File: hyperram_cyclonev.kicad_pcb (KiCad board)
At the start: 2 copper layers, 90.1 x 89.7 mm, 57 parts, among them IC1 AP63205WU, IC2 TXB0108PWR, IC3 S26KL128SDABHI020, IC4 W25Q32JVSSIQ_TR, IC5 S27KL0641DABHI020, J1 ASP-122952-01, J2 HDMI_A, J3 Conn_02x10_Odd_Even, J4 Conn_02x06_Odd_Even, J5 Conn_02x06_Top_Bottom, J6 Conn_02x06_Top_Bottom, J7 Conn_02x06_Top_Bottom, Q1 BSS138, Q2 BSS138

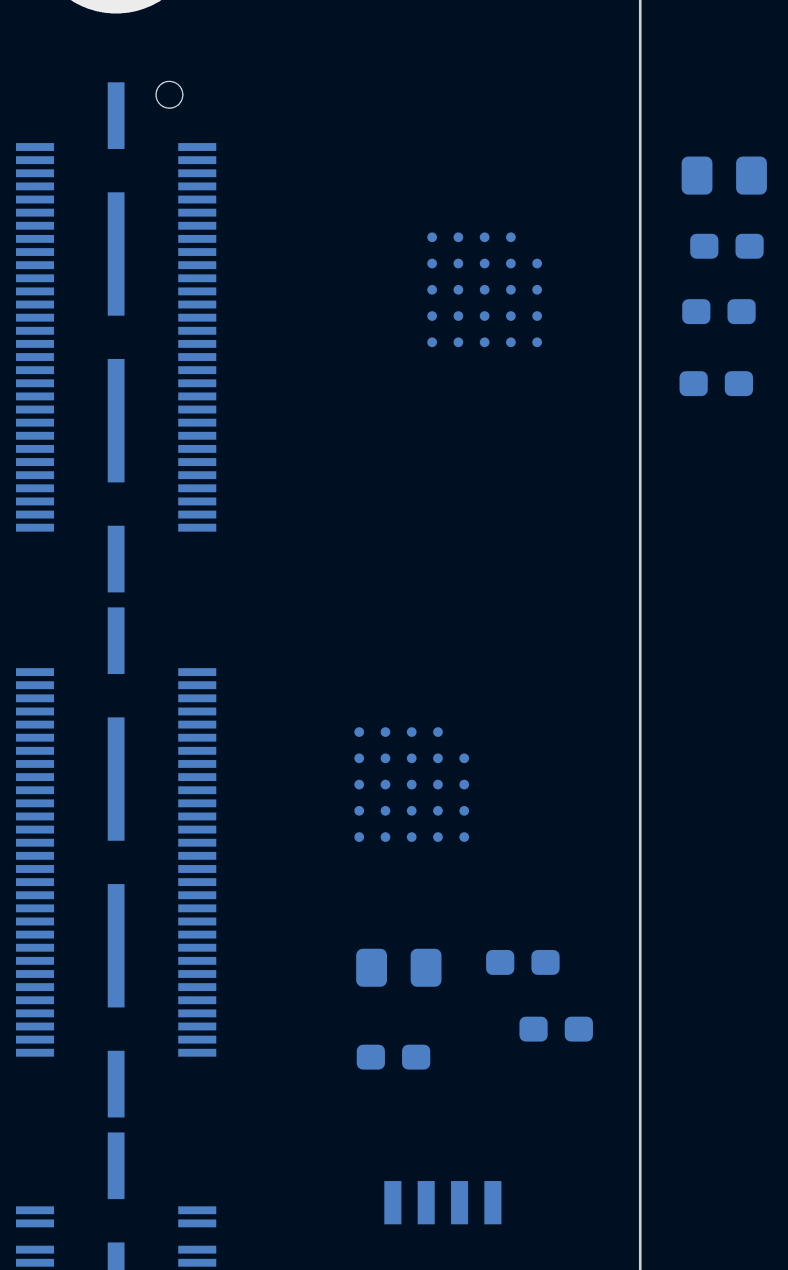
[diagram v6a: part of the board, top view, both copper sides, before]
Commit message: Set constraints for PCBWay: 6/6mil, hole 0.25mm. First try for routing HyperRAM with trace length matching.
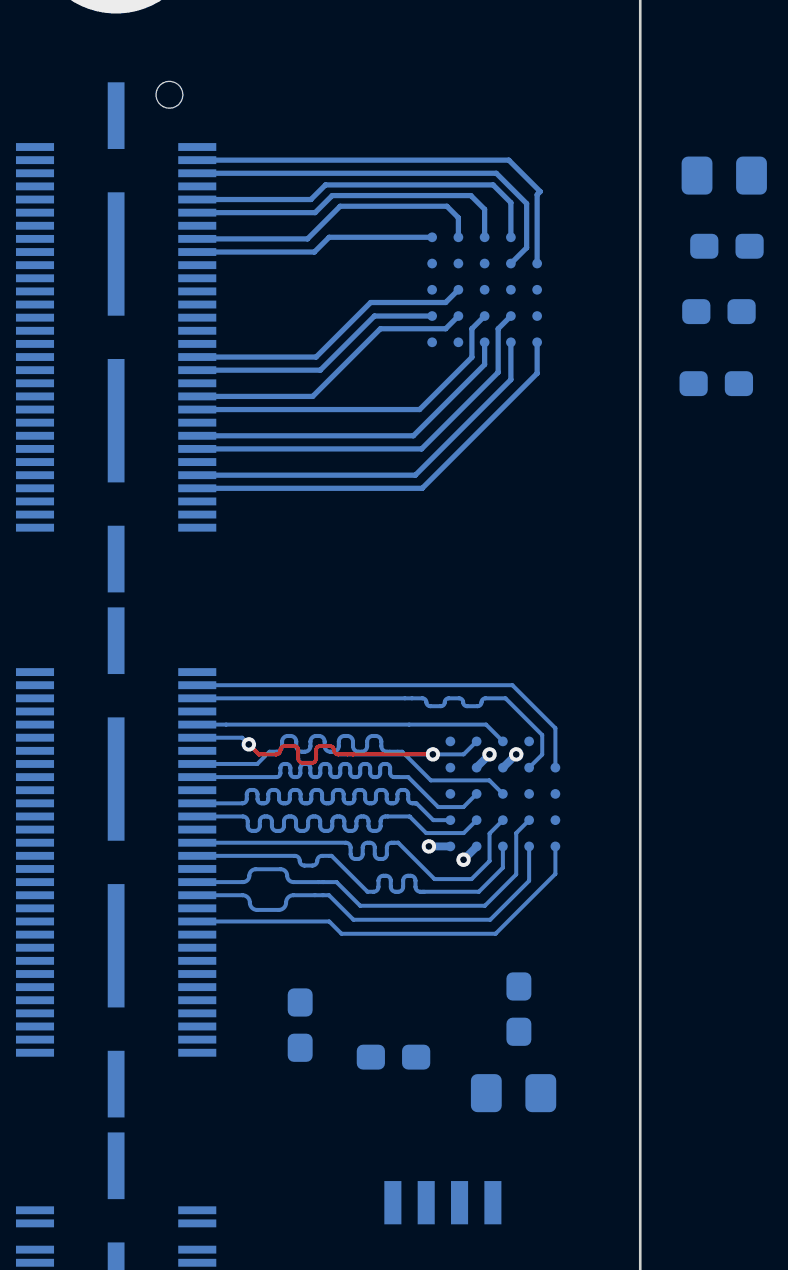
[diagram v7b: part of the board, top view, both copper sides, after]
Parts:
- moved C15 9.75 mm to (229.5, 119.4), turned to -90 degrees
- moved C11 6.47 mm to (237.6, 122.0)
- moved IC5 3.49 mm to (237.2, 110.6)
- moved C14 1.78 mm to (237.8, 118.8), turned to 90 degrees
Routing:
- net /hr2_clkn: track 0.00 -> 16.3 mm
- net /hr2_dq7: track 0.00 -> 15.9 mm
- net /hr1_dq7: track 0.00 -> 15.8 mm
- net /hr1_clkn: track 0.00 -> 15.8 mm
- net /hr1_dq1: track 0.00 -> 15.8 mm
- net /hr1_clkp: track 0.00 -> 15.8 mm
- net /hr1_rwds: track 0.00 -> 15.7 mm
- net /hr1_dq3: track 0.00 -> 15.6 mm
- net /hr1_dq2: track 0.00 -> 15.6 mm
- net /hr1_dq4: track 0.00 -> 15.6 mm
- net /hr2_clkp: track 0.00 -> 15.6 mm
- net /hr1_dq0: track 0.00 -> 15.6 mm
- net /hr1_dq6: track 0.00 -> 15.5 mm
- net /hr1_dq5: track 0.00 -> 15.5 mm
- net /hr2_dq1: track 0.00 -> 15.0 mm
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
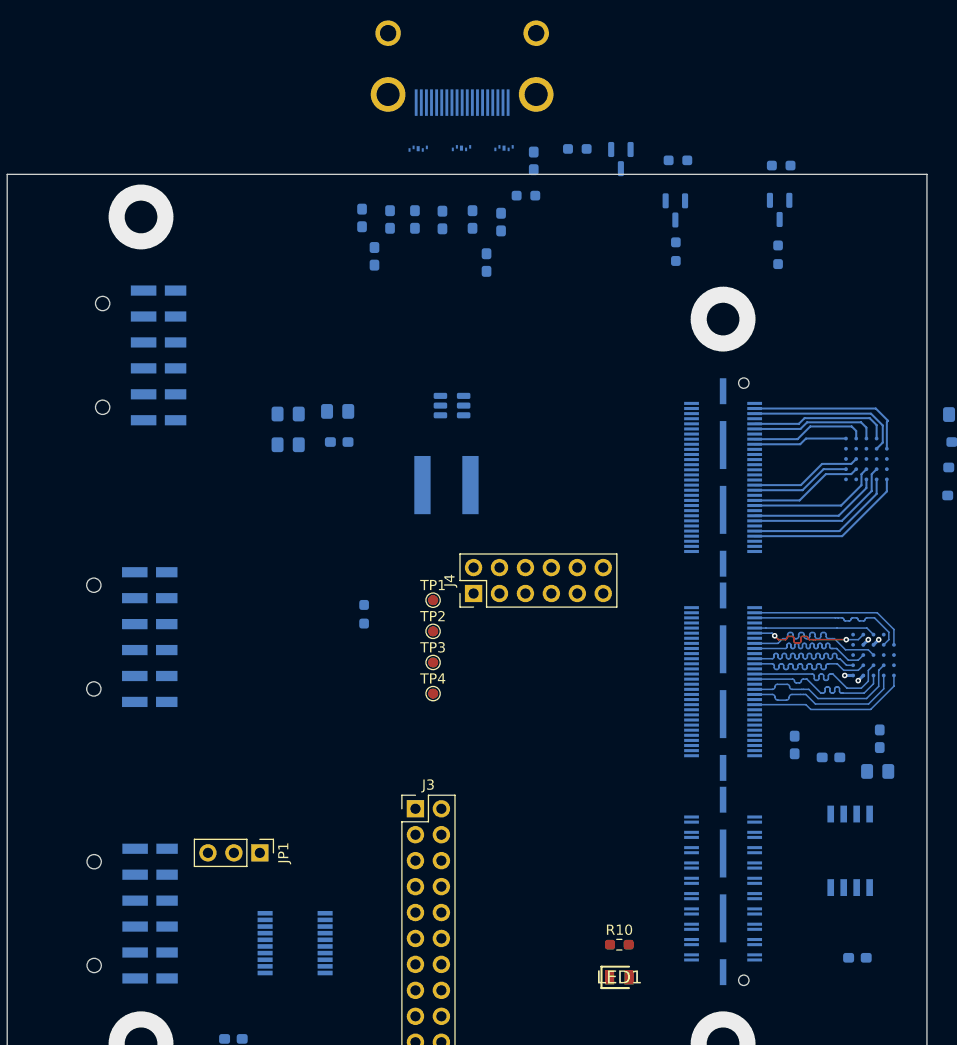
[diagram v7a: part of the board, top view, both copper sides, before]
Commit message: Optimizing signal assigments and component placement to simplify routing.
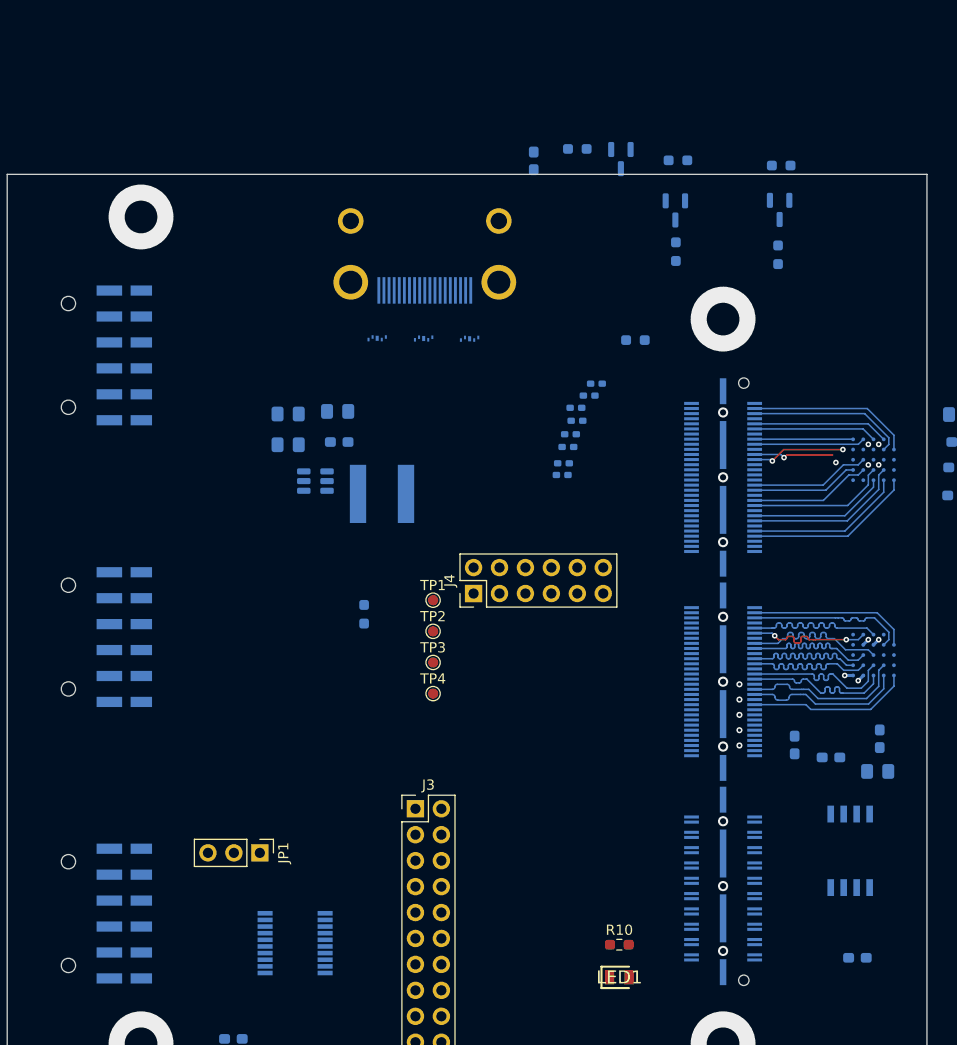
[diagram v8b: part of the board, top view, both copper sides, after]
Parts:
- C17, C18, C19, C20, C21, C22, C23, C24: footprint Capacitor_SMD:C_0603_1608Metric_Pad1.08x0.95mm_HandSolder -> Capacitor_SMD:C_0402_1005Metric_Pad0.74x0.62mm_HandSolder
- moved C24 28.0 mm to (208.1, 86.4), turned to 180 degrees
- moved C23 26.9 mm to (208.2, 87.6), turned to 180 degrees
- moved C20 26.6 mm to (206.9, 91.8), turned to 180 degrees
- moved C21 26.6 mm to (207.3, 90.2), turned to 180 degrees
- moved C22 26.0 mm to (207.6, 89.0), turned to 180 degrees
- moved D2 22.4 mm to (188.6, 79.6), turned to -90 degrees
- moved C19 22.1 mm to (206.7, 92.9), turned to 180 degrees
- moved C17 20.7 mm to (209.4, 85.2), turned to 180 degrees
- moved D4 19.3 mm to (197.7, 79.6)
- moved D1 19.0 mm to (193.2, 79.6)
- moved J2 18.7 mm to (193.3, 75.7)
- moved C18 18.4 mm to (210.1, 84.0), turned to 180 degrees
- moved R6 17.7 mm to (213.9, 79.7)
- moved IC1 15.3 mm to (182.6, 93.5)
- moved L1 6.37 mm to (189.1, 94.8)
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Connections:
- D1 pad 2: /xhdmi_d0n -> /xhdmi_d0p
- D1 pad 4: /xhdmi_d0p -> /xhdmi_clkp
- D1 pad 5: /xhdmi_clkp -> /xhdmi_d0n
- D2 pad 1: /cec -> /hpdet
- D2 pad 2: /hpdet -> /cec
- D2 pad 4: /ddc_clk -> /ddc_dat
- D2 pad 5: /ddc_dat -> /ddc_clk
- D4 pad 2: /xhdmi_d2n -> /xhdmi_d2p
- D4 pad 4: /xhdmi_d2p -> /xhdmi_d1p
- D4 pad 5: /xhdmi_d1p -> /xhdmi_d2n
- J1 pad 131: /hf_psc -> /hr2_rwds
- J1 pad 133: /hf_pscn -> /hf_csn
- J1 pad 137: /hr2_rwds -> /hf_psc
- J1 pad 139: /hf_csn -> /hf_pscn
- J1 pad 143: /hf_intn -> /hr2_rstn
- J1 pad 145: /hr2_rstn -> /hf_intn
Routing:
- net /hf_psc: track 0.00 -> 9.16 mm, vias 0 -> 2
- net /hf_pscn: track 0.00 -> 7.89 mm, vias 0 -> 2
- net /hr1_csn: track 11.9 -> 15.6 mm
- net /hr2_dq4: track 9.80 -> 10.5 mm
- net /hr2_dq2: track 11.0 -> 11.7 mm
- net /hr2_dq3: track 11.2 -> 11.9 mm
- net /hr2_dq0: track 13.1 -> 13.6 mm
- net /hr2_dq5: track 12.9 -> 13.5 mm
- net /hr2_rstn: track 11.4 -> 10.8 mm
- net /hr2_dq7: track 15.9 -> 16.5 mm
- net /hr2_dq1: track 15.0 -> 15.5 mm
- net /hr2_dq6: track 14.9 -> 15.4 mm
- net /hf_rston: track 13.8 -> 13.3 mm
- net GND: vias 2 -> 12
- net /hr2_rwds: vias 0 -> 1
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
